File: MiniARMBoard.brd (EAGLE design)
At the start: 35.6 x 20.6 mm, 39 parts, among them CN1 J_USB_MICROAB_HIROSE_ZX62-AB-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, U1 LPC1549JBD48, U2 TPD4S014DSQR, U3 MCP1700T-33, U4 ADR5041, U5 FT234XD-R, X1 FA238V

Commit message: 回路図の見た目を整えてみた
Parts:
- CN1: value J_USB_MICROAB_HIROSE_ZX62-AB-5PA -> ZX62-AB-5PA
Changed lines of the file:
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@@
 <?xml version="1.0" encoding="utf-8"?>
 <!DOCTYPE eagle SYSTEM "eagle.dtd">
-<eagle version="8.4.3">
+<eagle version="8.6.3">
 <drawing>
 <settings>
@@
 <param name="checkRestrict" value="0"/>
 <param name="checkStop" value="0"/>
+<param name="checkValues" value="0"/>
 <param name="useDiameter" value="13"/>
 <param name="maxErrors" value="50"/>
@@
 <attribute name="VALUE" x="16.7308" y="14.1194" size="0.8" layer="27" font="vector" ratio="18"/>
 </element>
-<element name="CN1" library="j_usb_hirose_zx62-ab-5pa" library_urn="urn:adsk.eagle:library:1080482" package="J_USB_MICROAB_HIROSE_ZX62-AB-5PA" package3d_urn="urn:adsk.eagle:package:1080486/2" value="J_USB_MICROAB_HIROSE_ZX62-AB-5PA" x="0.127" y="10.16" smashed="yes" rot="R270">
+<element name="CN1" library="j_usb_hirose_zx62-ab-5pa" library_urn="urn:adsk.eagle:library:1080482" package="J_USB_MICROAB_HIROSE_ZX62-AB-5PA" package3d_urn="urn:adsk.eagle:package:1080486/2" value="ZX62-AB-5PA" x="0.127" y="10.16" smashed="yes" rot="R270">
 <attribute name="NAME" x="2.6966" y="5.0746" size="0.8128" layer="25" font="vector" ratio="20"/>
 <attribute name="VALUE" x="5.247" y="9.775" size="1.016" layer="27" font="vector" ratio="20" rot="R270"/>

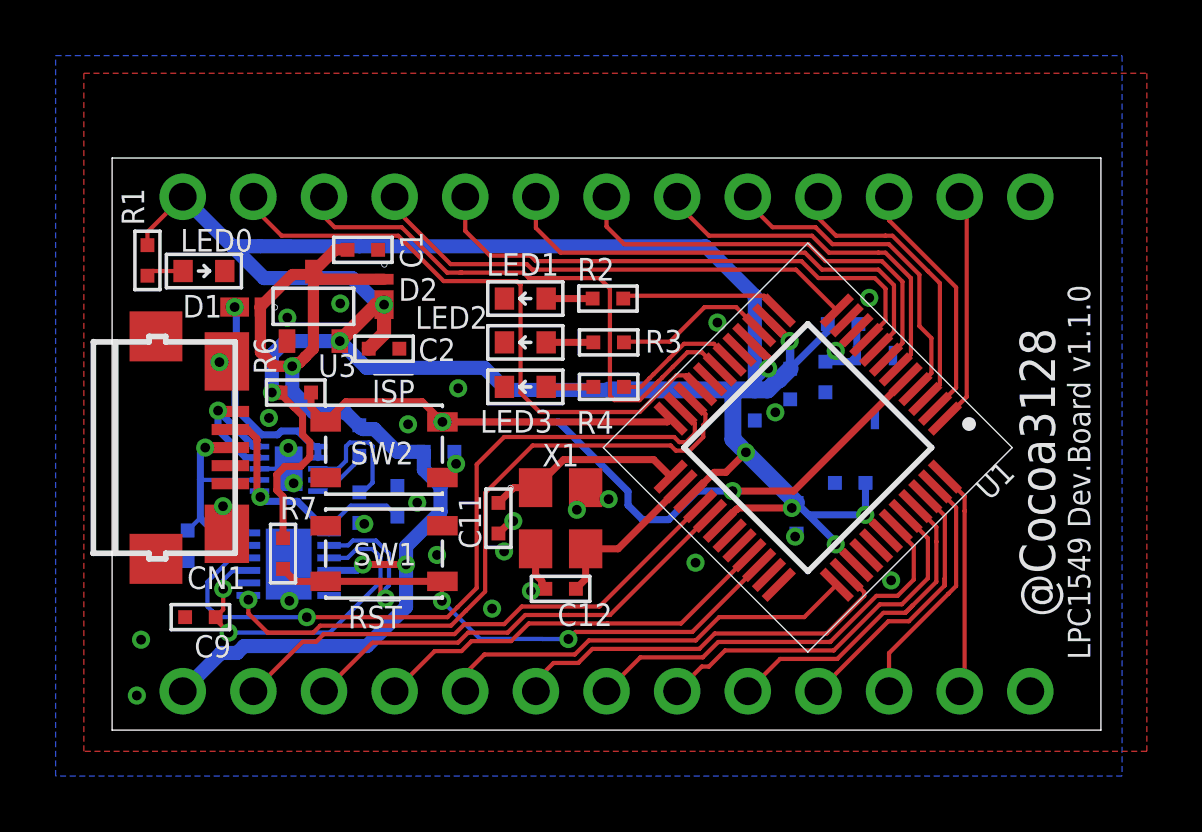
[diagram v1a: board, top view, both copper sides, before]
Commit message: [fix]usb-dfu仕様に変更
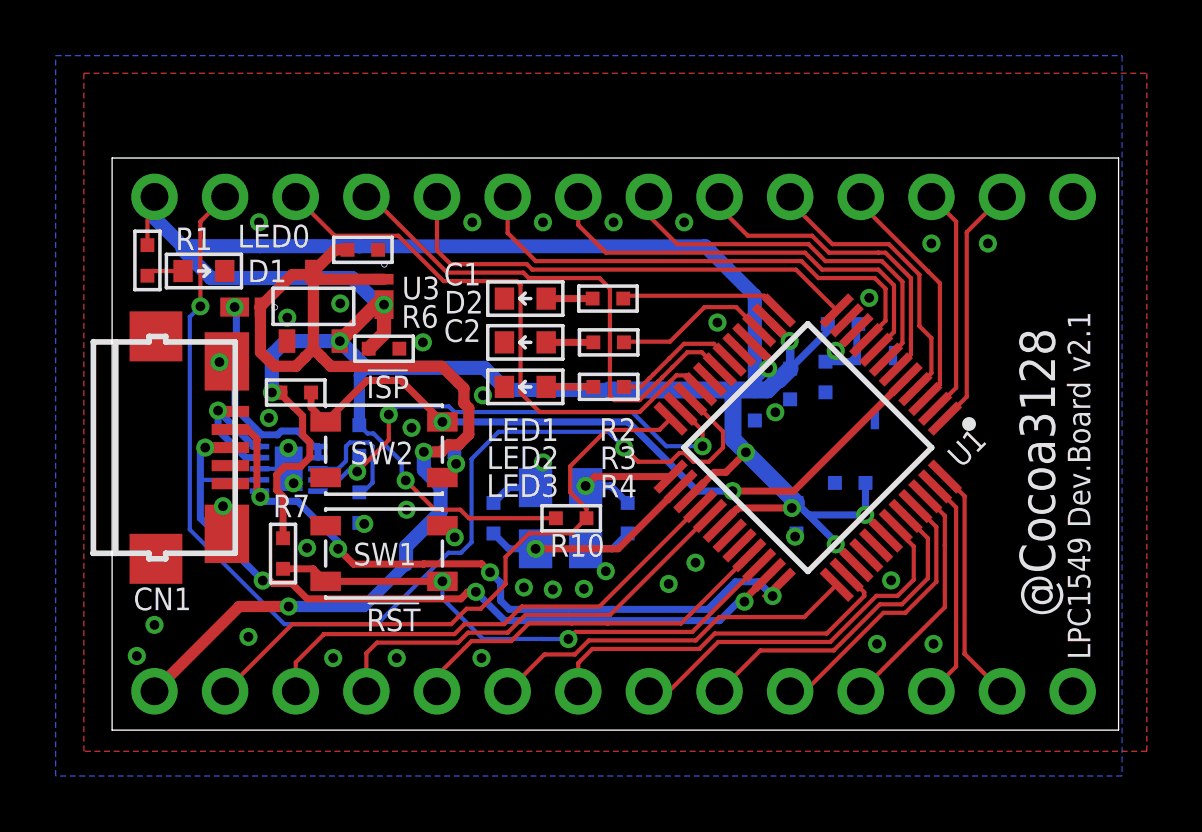
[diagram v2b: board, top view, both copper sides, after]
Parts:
- removed C7, C8: 47p, MotorDriver:C1005
- removed C9: 0.1u, MotorDriver:C1005
- removed U5: FT234XD-R, FT234XD-R:SON45P300X300X75-13N
- added R10: 10k, MotorDriver:R1005
- CN2, CN3: value (none) -> HEADER1X14; device nonolith:1X13_ROUND -> nonolith:1X14_ROUND
- R1, R2, R3, R4: value 220 -> 330
- moved C11 4.65 mm to (18.5, 7.62), flipped to the bottom
- moved C12 3.50 mm to (13.7, 7.62), flipped to the bottom, turned to 90 degrees
- moved CN3 1.52 mm to (18.0, 1.40), flipped to the top, turned to 0 degrees
- moved CN2 1.02 mm to (18.0, 19.2), flipped to the top, turned to 180 degrees
- flipped X1 to the bottom
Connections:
- removed net N$4: C9.1, U5.3, U5.9
- removed net N$7: R9.1, U2.4
- removed net RX: U1.22, U5.7
- removed net TX: U1.23, U5.10
- new net !ACK: R9.1, U1.23, U2.4
- new net PIO0_14: CN2.13, U1.22
- new net PIO0_16: CN3.2, R10.2, U1.24
- net !ISP: no longer U1.24
- net !RESET: no longer U5.2
- net +3V3: now also CN2.14, R10.1, R9.2; no longer CN2.13
- net +5V: no longer R9.2, U5.4
- net D+: now also U1.35; no longer C8.1, U5.12
- net D-: now also U1.36; no longer C7.1, U5.1
- net GND: now also CN3.14; no longer C7.2, C8.2, C9.2, CN3.13, U5.13, U5.5
- net PIO0_17: now also CN3.3; no longer CN3.2
- net PIO0_19: now also CN3.4; no longer CN3.3
- net PIO0_20: now also CN3.5; no longer CN3.4
- net PIO0_22: now also CN3.6; no longer CN3.5
- net PIO0_23: now also CN3.7; no longer CN3.6
- net PIO0_24: now also CN3.8; no longer CN3.7
- net PIO0_25: now also CN3.9; no longer CN3.8
- net PIO0_26: now also CN3.10; no longer CN3.9
- net PIO0_27: now also CN3.11; no longer CN3.10
- net PIO0_28: now also CN3.12; no longer CN3.11
- net PIO0_29: now also CN3.13; no longer CN3.12
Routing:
- net PIO0_14: track 0.00 -> 40.9 mm, vias 0 -> 2
- net TX: track 27.0 -> 0.00 mm, vias 1 -> 0
- net RX: track 24.1 -> 0.00 mm, vias 1 -> 0
- net PIO0_16: track 0.00 -> 22.6 mm
- net D+: track 8.23 -> 28.6 mm, vias 1 -> 4
- net !ACK: track 0.00 -> 18.4 mm, vias 0 -> 3
- net D-: track 9.65 -> 25.2 mm, vias 1 -> 4
- net +3V3: track 91.7 -> 105.6 mm, vias 9 -> 10
- net N$4: track 12.5 -> 0.00 mm, vias 2 -> 0
- net !ISP: track 34.8 -> 26.1 mm
- net !RESET: track 24.5 -> 19.7 mm, vias 3 -> 2
- net N$1: track 7.09 -> 5.03 mm, vias 0 -> 1
- net PIO0_12: track 21.0 -> 19.0 mm
- net N$2: track 5.93 -> 7.88 mm, vias 0 -> 1
- net N$7: track 1.93 -> 0.00 mm
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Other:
- board size 35.6 x 20.6 mm -> 36.2 x 20.6 mm
- board text added: "LPC1549 Dev.Board v2.1"
- board text removed: "LPC1549 Dev.Board v1.1.0"
